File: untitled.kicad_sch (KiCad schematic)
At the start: 21 parts, among them Q7 2N7000, Q8 2N7000, U3 L6387

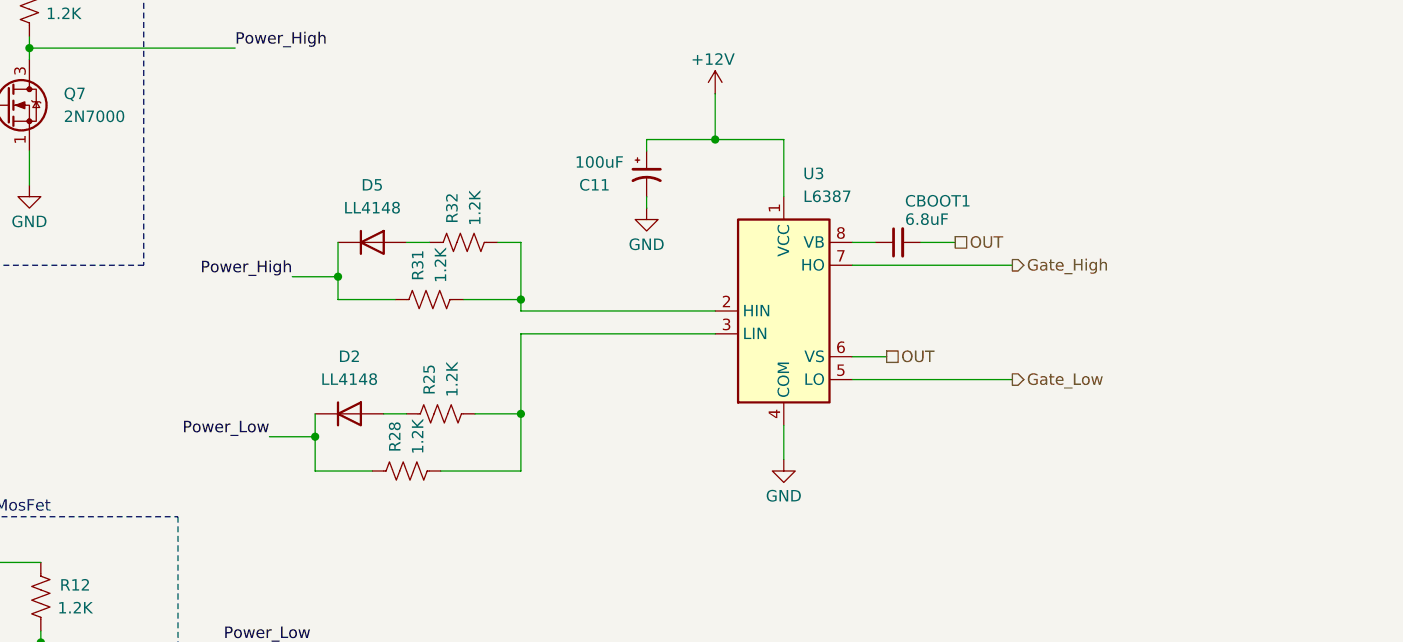
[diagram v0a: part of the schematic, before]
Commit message: posicion de las resistencias de gate corregidas
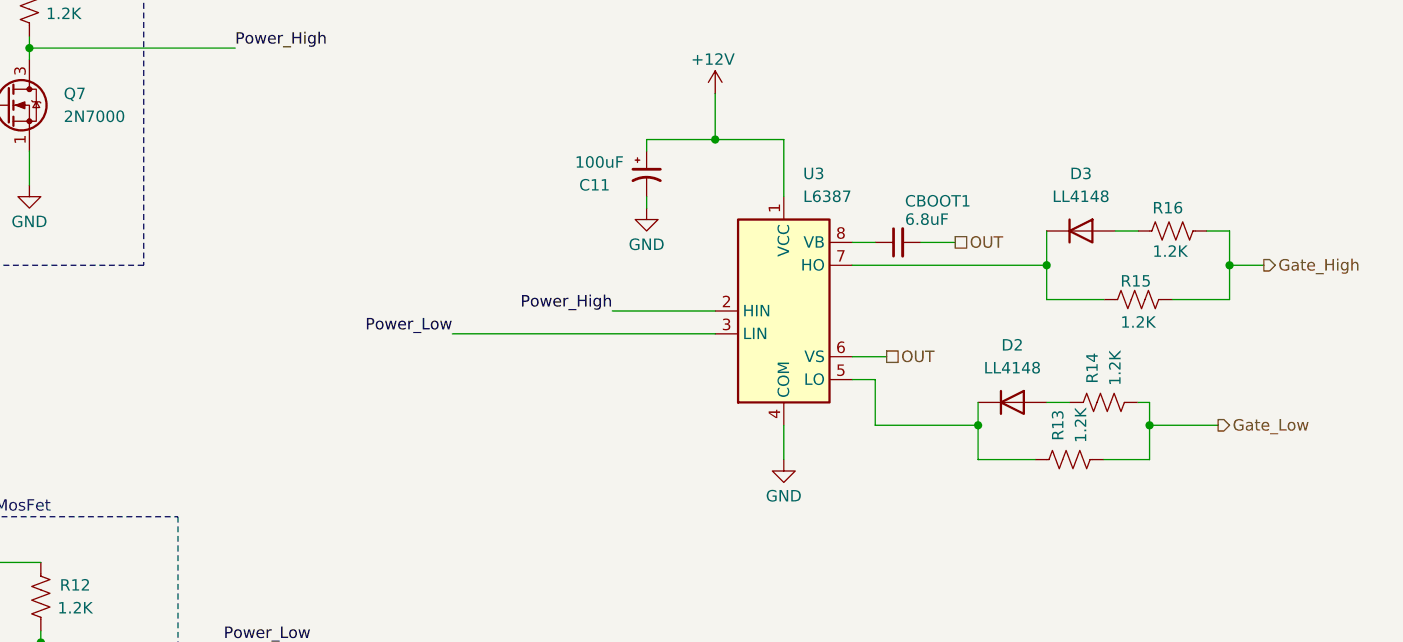
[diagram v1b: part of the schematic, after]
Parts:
- renumbered D5 to D3, R28 to R13, R25 to R14, R31 to R15, R32 to R16
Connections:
- net Gate_High: now also R15.2, R16.2; no longer U3.7 (HO)
- net Gate_Low: now also R13.2, R14.2; no longer U3.5 (LO)
- net Power_High: now also U3.2 (HIN); no longer D3.1 (K), R15.1
- net Power_Low: now also U3.3 (LIN); no longer D2.1 (K), R13.1
- new net: D2.1 (K), R13.1, U3.5 (LO)
- new net: D3.1 (K), R15.1, U3.7 (HO)
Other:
- moved on the sheet: D2, D3, R13, R14, R15, R16

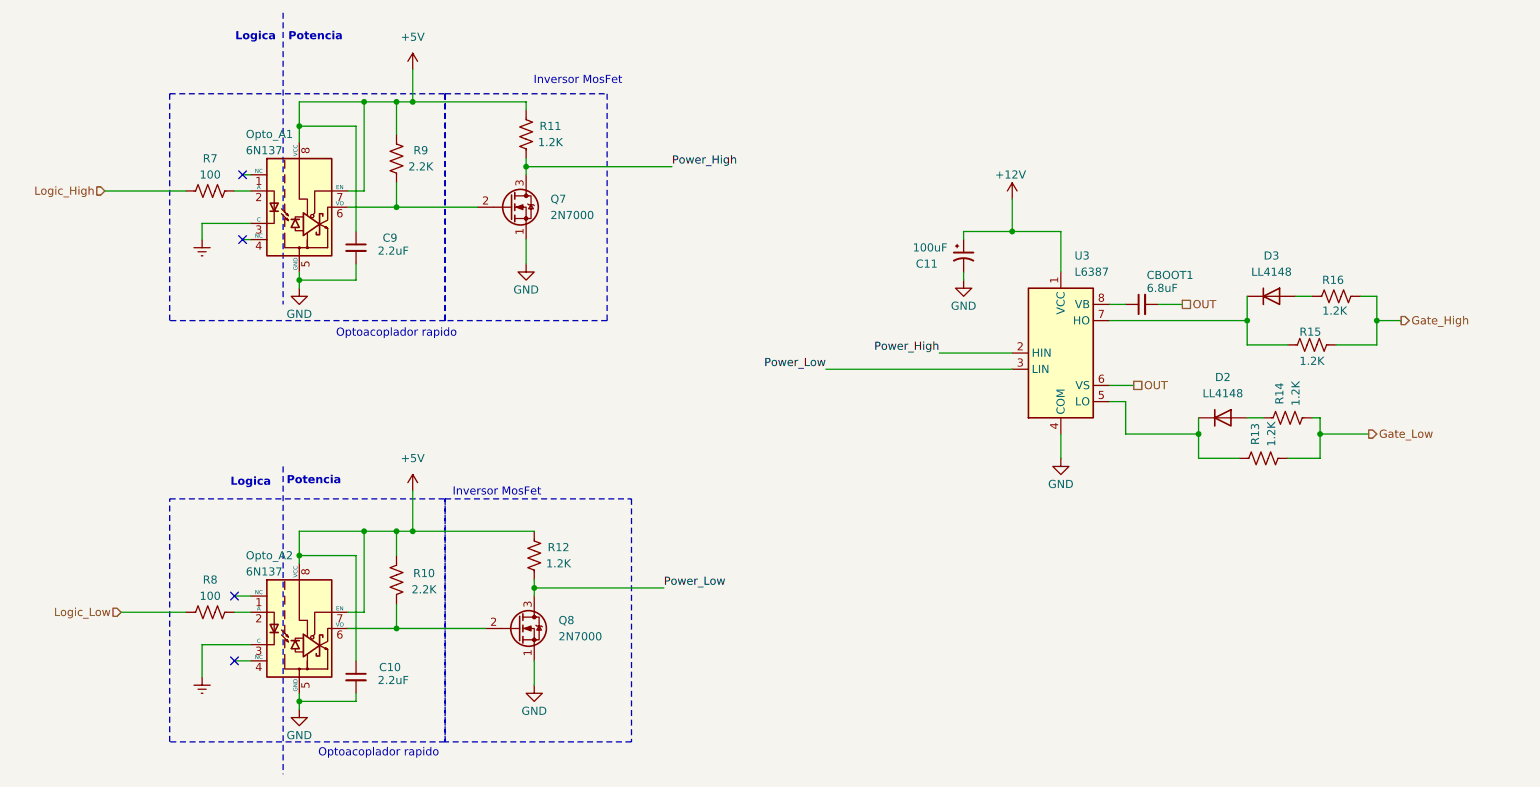
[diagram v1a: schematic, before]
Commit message: correciones( aislamiento LM7805) , cambio de ID , primer ruteo
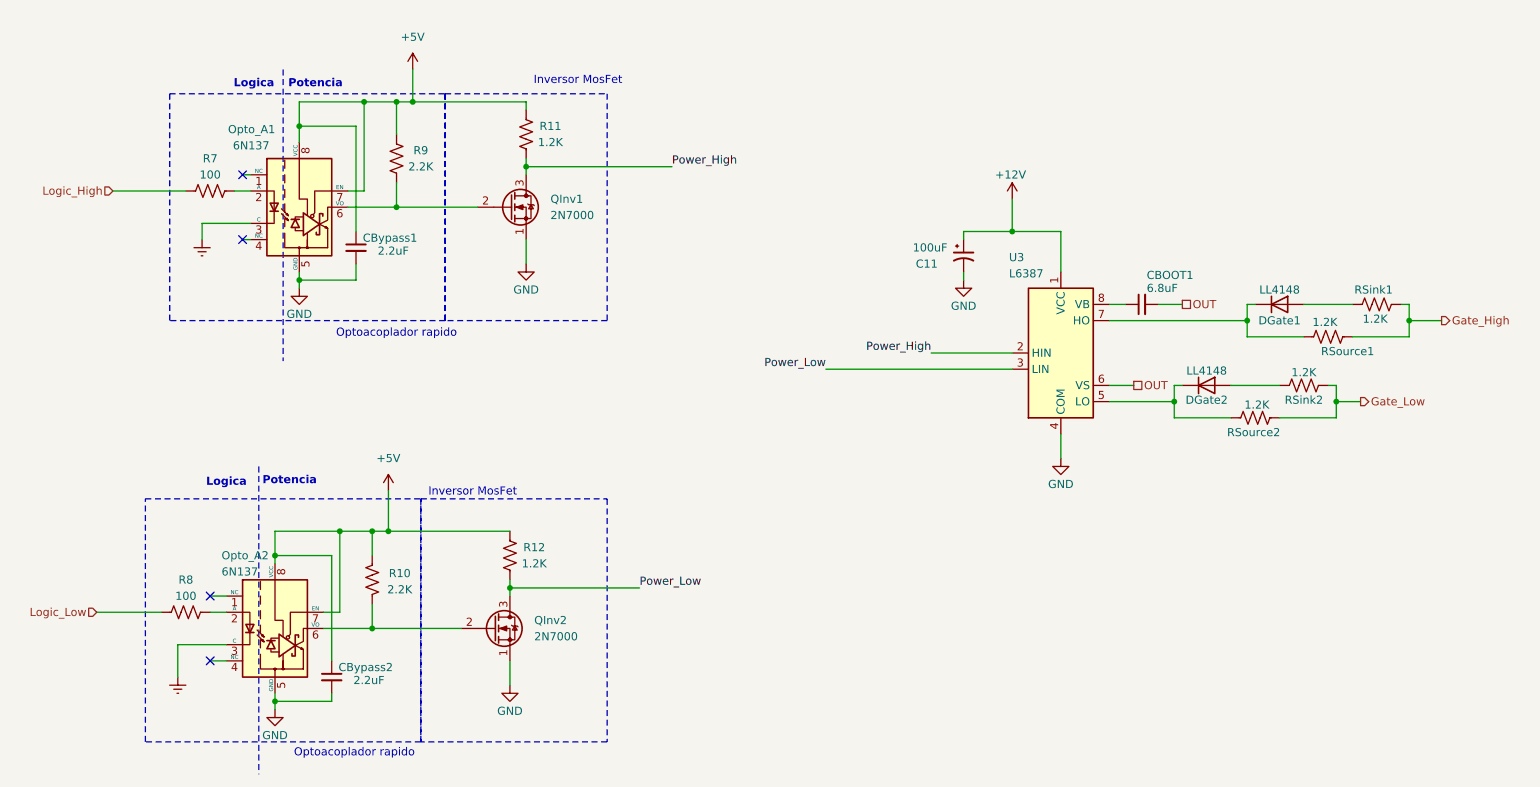
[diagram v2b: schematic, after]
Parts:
- renumbered C9 to CBypass1, C10 to CBypass2, D3 to DGate1, D2 to DGate2, Q7 to QInv1, Q8 to QInv2, R16 to RSink1, R14 to RSink2, R15 to RSource1, R13 to RSource2
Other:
- moved on the sheet: CBypass2, DGate1, DGate2, Opto_A2, QInv2, R10, R12, R8, RSink1, RSink2, RSource1, RSource2
